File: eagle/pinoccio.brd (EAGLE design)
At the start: 25.4 x 50.8 mm, 96 parts, among them J1 AVR_SPI_PRG_6, J2 AVR_SPI, J3 Switch, J4 Ext Battery, Q1 PFET, U1 MCP73832, U2 STLQ015XX, U3 ATMEGA16U2, U4 ATMEGA256RFR2, U5 MAX17048, U7 SWITCH, U8 LED-RGB, X1 16MHz, X2 32.768k, X3 16MHz, Y1 ANTENNA2SMD5

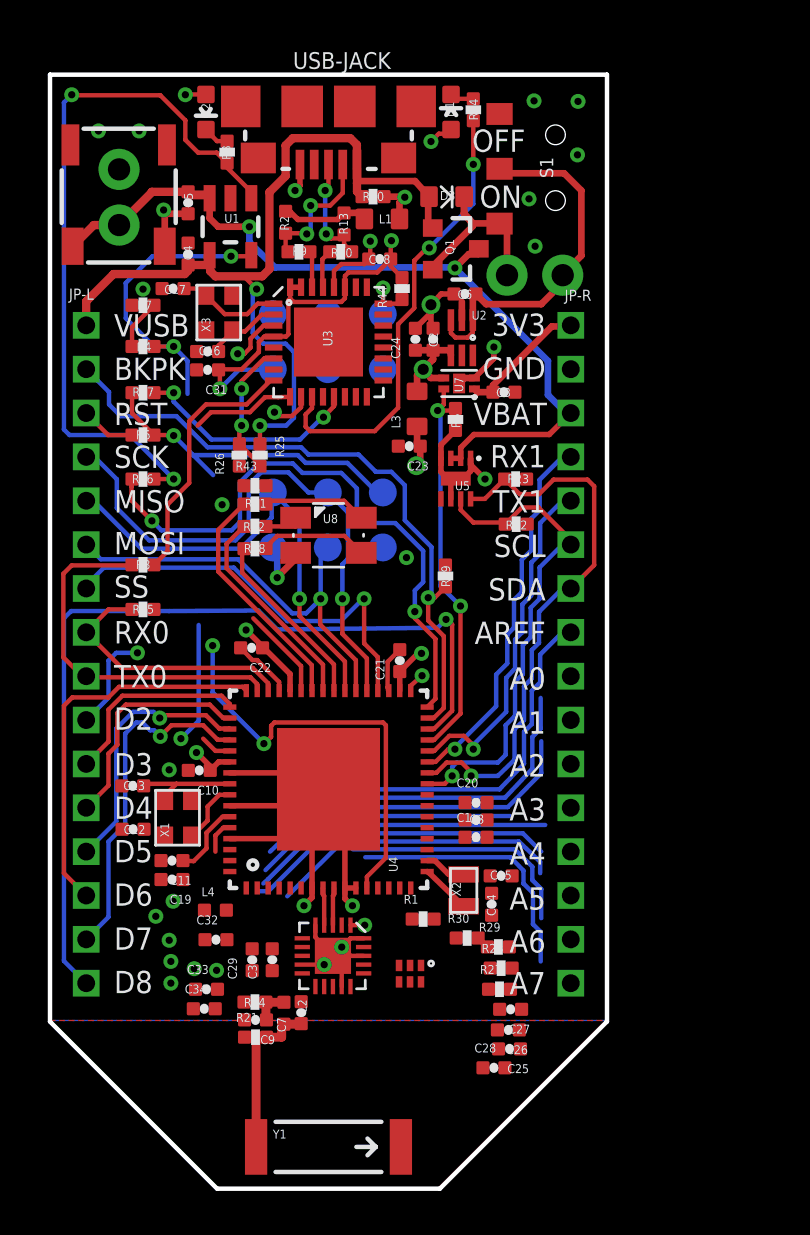
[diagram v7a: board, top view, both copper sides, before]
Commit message: Updated 256RFR2 to have vias under paddle, also more layout and fixes for GND vs AGND
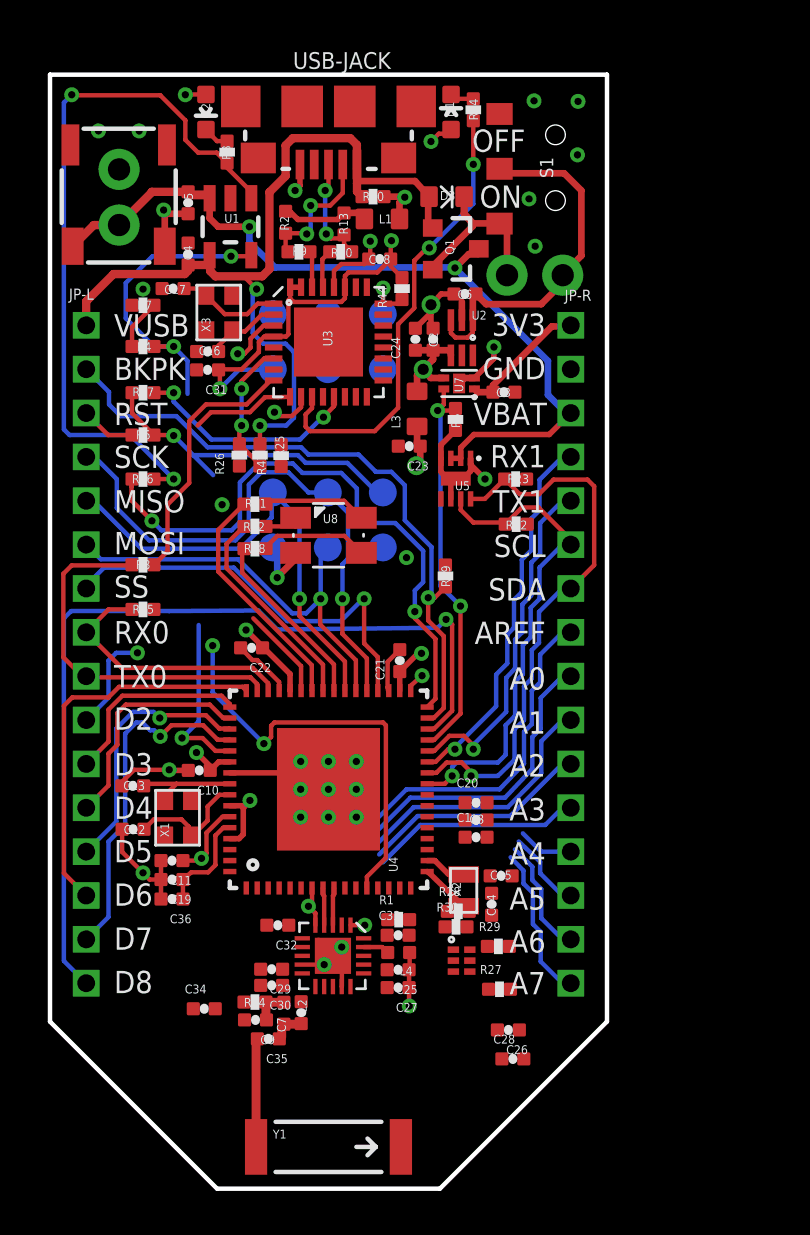
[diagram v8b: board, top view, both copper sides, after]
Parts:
- removed R21: DNI, Pinoccio:0402-RES
- removed U$18: INVERTER-DUALPAK, Pinoccio:MICROPAK
- added C35: DNI, Pinoccio:0402-CAP
- added C36: 20pF, Pinoccio:0402-CAP
- added U10: INVERTER-DUALPAK, Pinoccio:MICROPAK
- C19: value 1.0uF -> 0.1uF
- C23, C24: value 0.1uF -> 1.0uF
- C29, C30: value 22pF -> 20pF
- L2: value 4.7nH -> 2.7nH
- R1: value 2k -> 2K
- R20, R5: value 100k -> 100K
- U4: device Pinoccio:QFN-64 -> Pinoccio:QFN-64-256RFR2
- moved C33 9.08 mm to (15.9, 11.6)
- moved L4 8.58 mm to (15.9, 10.8), turned to 180 degrees
- moved C25 6.23 mm to (15.9, 9.98)
- moved C27 5.23 mm to (15.9, 9.17)
- moved R28 3.25 mm to (18.6, 12.6)
- moved C32 2.90 mm to (10.4, 12.0), turned to 180 degrees
- moved R43 1.82 mm to (10.5, 33.4), turned to 90 degrees
- moved C30 1.17 mm to (10.1, 9.27), turned to 180 degrees
- moved R1 1.12 mm to (15.9, 12.3)
- moved C29 0.99 mm to (10.1, 10.0), turned to 180 degrees
- moved C28 0.95 mm to (21.1, 5.92)
- moved R30 0.72 mm to (18.5, 11.9)
- renumbered U$17 to U9
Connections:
- removed net A0-IN: JP-R.P$9
- removed net A1-IN: JP-R.P$10
- removed net A2-IN: JP-R.P$11
- removed net A3-IN: JP-R.P$12
- removed net A4-IN: JP-R.P$13
- removed net A5-IN: JP-R.P$14
- removed net A6-IN: JP-R.P$15
- removed net A7-IN: JP-R.P$16
- removed net AGND: C33.2, C34.2
- removed net AVCC: C11.1, C23.1, C25.1, C26.1, C27.1, C28.1, C32.1, C33.1, C34.1, L3.1, L4.1, U$18.P$5, U4.59, U9.1, U9.6
- net A0: now also JP-R.P$9
- net A1: now also JP-R.P$10
- net A2: now also JP-R.P$11
- net A3: now also JP-R.P$12
- net A4: now also JP-R.P$13
- net A5: now also JP-R.P$14
- net A6: now also JP-R.P$15
- net A7: now also JP-R.P$16
- net ANT: now also C35.1; no longer R21.2
- net AVDD: now also C36.1; no longer U9.2
- net CRX: now also U10.P$3, U10.P$6; no longer U$18.P$3, U$18.P$6
- net CTX: now also U10.P$4; no longer U$18.P$4
- net GND: now also C33.2, C34.2, C35.2, C36.2, U10.P$2, U4.GND$1, U4.GND$2, U4.GND$3, U4.GND$4, U4.GND$5, U4.GND$6, U4.GND$7, U4.GND$8, U4.GND$9, U9.GND, U9.GND$1; no longer R21.1, U$18.P$2, U9.P$1, U9.P$2
- net N$10: now also U10.P$1; no longer U$18.P$1
- net VCC: now also C11.1, C23.1, C25.1, C26.1, C27.1, C28.1, C32.1, C33.1, C34.1, L3.1, L4.1, U10.P$5, U4.59, U9.1, U9.6
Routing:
- net GND: track 64.3 -> 53.5 mm, vias 21 -> 22
- net A5: track 13.5 -> 3.69 mm
- net VCC: track 36.0 -> 44.6 mm, vias 9 -> 13
- net A4: track 9.56 -> 2.53 mm, vias 1 -> 0
- net AVCC: track 5.96 -> 0.00 mm, vias 2 -> 0
- net A6: track 11.0 -> 5.38 mm, vias 1 -> 0
- net A7: track 11.9 -> 7.10 mm
- net A3: track 14.3 -> 9.59 mm, vias 1 -> 0
- net A1: track 15.9 -> 12.2 mm, vias 1 -> 0
- net AVDD: track 1.54 -> 4.78 mm
- net AREF: track 18.7 -> 15.6 mm, vias 1 -> 0
- net X1_P: track 3.15 -> 6.17 mm
- net A0: track 16.9 -> 14.0 mm, vias 1 -> 0
- net A2: track 12.5 -> 10.4 mm, vias 1 -> 0
- net N$3: track 0.00 -> 1.20 mm
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- removed copper zone on layer 16, net N$12
- removed copper zone on layer 1, net N$2
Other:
- board text added: "2015-03-14"
- board text added: "Layout Notes: RFN and RFP are a differential pair. They need to be routed parallel to work. Atmel recommends using 12 mil traces with an 8 mil gap and an 11 mil dielectric"
- board text removed: "2013-08-15"
